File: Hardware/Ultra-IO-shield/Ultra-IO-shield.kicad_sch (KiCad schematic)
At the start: 88 parts, among them J1 Conn_01x04, J10 ASSMANN_A-DF_09_PP/Z, J11 TC_1578891_SCART, J12 Conn_01x01, J13 Conn_01x02, J14 CUI_SD-50BV, J15 Conn_01x02, J16 CUI_SD-50BV, J17 CUI_SD-50BV, J18 Conn_01x04, J19 Conn_01x04, J2 DIN-8_SD-80BV, J20 Conn_01x02, J21 ASSMANN_A-DF_09_PP/Z, J22 Conn_01x02, J3 Conn_01x04, J4 Conn_01x06, J5 Conn_01x02, J6 Conn_RCJ-023, J7 Conn_RCJ-022, J8 Conn_01x02, J9 NorComp_111-014-213L001, Q1 MMBT2907AM3T5G, U1 LM211, U2 AP7370, U3 ADuM226

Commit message: Redesigning of the IO-shield, to make room for Keyboard, power and USB.
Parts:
- added C?: C_GRM21BR61A476ME15K, Capacitor_SMD:C_0805_2012Metric, symbol LRJ-parts:C_GRM21BR61A476ME15K
- added J?: AdamTech_USB3-2_USB_C_Receptacle, LRJ:USB_3-2_Receptacle_A3-C31-D-RA-CS1, symbol LRJ-parts:AdamTech_USB3-2_USB_C_Receptacle
- added R?: R_ERJ-3GEYJ105V, Resistor_SMD:R_0603_1608Metric, symbol LRJ-parts:R_ERJ-3GEYJ105V
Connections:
- net +5V: now also J?.1 (VBUS[1]), J?.A4 (VBUS[2]), J?.A9 (VBUS), J?.B4 (VBUS), J?.B9 (VBUS)
- net GND: now also C?.2, J?.7 (DRAIN), R?.1
- new net: J?.4 (GND), J?.A1 (GND), J?.A12 (GND), J?.B1 (GND), J?.B12 (GND), R?.2
- new net: C?.1, J?.SH (SHIELD)
- new net AUX+: J?.A8 (SBU1)
- new net AUX-: J?.B8 (SBU2)
- new net CC1/HPD: J?.A5 (CC1)
- new net RX1+: J?.B11 (RX1+)
- new net RX1-: J?.B10 (RX1-)
- new net SSRX+: J?.6 (SSRX+)
- new net SSRX-: J?.5 (SSRX-)
- new net SSTX+: J?.9 (SSTX+)
- new net SSTX-: J?.8 (SSTX-)
- new net TX1+: J?.A2 (TX1+)
- new net TX1-: J?.A3 (TX1-)
- new net USB1_D+: J?.3 (D+)
- new net USB1_D-: J?.2 (D-)
- new net USB2_D+: J?.A7 (D-)
- new net USB2_D-: J?.A6 (D+)
- no-connect marks 21 -> 28
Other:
- note added: "USB connector"

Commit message: Multiple redesigns of the IO-shield. Replaced FPGA with lower pin-count AT10K, since the higher pin-count one is now obsolete.
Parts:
- removed J13, J20: Conn_01x02, Connector_PinHeader_1.27mm:PinHeader_1x02_P1.27mm_Horizontal, symbol Connector_Generic:Conn_01x02
- removed J4: Conn_01x06, Connector_PinHeader_1.27mm:PinHeader_1x06_P1.27mm_Horizontal, symbol Connector_Generic:Conn_01x06
- removed J?: AdamTech_USB3-2_USB_C_Receptacle, LRJ:USB_3-2_Receptacle_A3-C31-D-RA-CS1, symbol LRJ-parts:AdamTech_USB3-2_USB_C_Receptacle
- removed TP1, TP2: TestPoint_2Pole, NetTie:NetTie-2_SMD_Pad0.5mm, symbol Connector:TestPoint_2Pole
- added C14, C16: C_CL10B104KB8NNNL, LRJ:C_0603_1608Metric_round_court, symbol LRJ-parts:C_CL10B104KB8NNNL
- added C15: C_GRM21BR61A476ME15K, Capacitor_SMD:C_0805_2012Metric, symbol LRJ-parts:C_GRM21BR61A476ME15K
- added F2, F3: PPTC_0603L075, Fuse:Fuse_0603_1608Metric, symbol LRJ-parts:PPTC_0603L075
- added J13: Conn_01x01, LRJ:PinHeader_1x01_P2.54mm_Horizontal_less-silk, symbol Connector_Generic:Conn_01x01
- added J20, J29, J31, J32, J4: Conn_01x02, LRJ:PinHeader_1x01_P1.27mm_Horizontal_less-silk, symbol Connector_Generic:Conn_01x01
- added J23, J24: USB_C_GCT_USB4115-03-C, LRJ:USB_C_Receptacle_GCT_USB4115-03-C, symbol LRJ-parts:USB_C_GCT_USB4115-03-C
- added J25: Conn_01x02, LRJ:PinHeader_1x02_P1.27mm_Horizontal_less-silk, symbol Connector_Generic:Conn_01x02
- added J26, J27, J28, J30: BC075-06, LRJ:GCT_BC075-06_PinHeader_1x06_P1.00mm_Horizontal_SMD, symbol LRJ-parts:BC075-06
- added R40: R_ERJ-3GEYJ105V, Resistor_SMD:R_0603_1608Metric, symbol LRJ-parts:R_ERJ-3GEYJ105V
- added TP1, TP2: NetTie-2_small_round, NetTie:NetTie-2_SMD_Pad0.5mm, symbol LRJ-parts:NetTie-2_small_round
- C1, C12, C3, C5, C7: Mounting Type SMD -> (none); Mounting type (none) -> SMD; Voltage Rating (none) -> 50V; Voltage Rating  50V -> (none)
- C11, C9: value C -> 22nF
- C13: renamed from C?; Capacitance (none) -> 47uF; Capacity 47uF -> (none)
- F1: footprint Fuse:Fuse_1812_4532Metric -> LRJ:Yageo_Fuse_1812_4532Metric
- J12: footprint Connector_PinHeader_1.27mm:PinHeader_1x01_P1.27mm_Horizontal -> LRJ:PinHeader_1x01_P2.54mm_Horizontal_less-silk
- J15: footprint Connector_PinHeader_1.27mm:PinHeader_1x02_P1.27mm_Horizontal -> LRJ:PinHeader_1x01_P1.27mm_Horizontal_less-silk; symbol Connector_Generic:Conn_01x02 -> Connector_Generic:Conn_01x01
- J19: value Conn_01x04 -> Conn_01x03; footprint LRJ:PinHeader_1x04_P2.54mm_Horizontal_less-silk -> LRJ:PinHeader_1x03_P2.54mm_Horizontal_less-silk; symbol Connector_Generic:Conn_01x04 -> Connector_Generic:Conn_01x03
- J22, J5, J8: footprint Connector_PinHeader_1.27mm:PinHeader_1x02_P1.27mm_Horizontal -> LRJ:PinHeader_1x02_P1.27mm_Horizontal_less-silk
- R11, R23: value R -> 1K
- R12: value R -> 220K; footprint Resistor_SMD:R_0805_2012Metric -> LRJ:R_0805_2012Metric_roundcourt
- R13, R21, R22: value R -> 4.7K
- R14, R18: value R -> 10K
- R15, R16: value R -> 2.7K
- R17: value R -> 470K
- R20: value R -> 100R
- R8: footprint Resistor_SMD:R_0603_1608Metric -> LRJ:C_0603_1608Metric_round_court
- U3: footprint Package_SO:SOIC-8_7.5x5.85mm_P1.27mm -> LRJ:TEXAS_RI-8-1_7.5x5.85mm_P1.27mm
- gave numbers to parts that had none: 1
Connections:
- net +12V: now also J13.1 (Pin_1); no longer J19.1 (Pin_1)
- net +5V: now also J19.1 (Pin_1), C14.1, C16.1, F2.2, F3.2, J25.1 (Pin_1); no longer J15.2 (Pin_2), J19.2 (Pin_2)
- net +5VD: now also TP2.2
- net +5VD_: now also TP2.1
- net CC1/HPD: now also J23.A5 (CC1), J23.B5 (CC2), J27.2 (Pin_2)
- net GND: now also C14.2, C15.2, C16.2, J25.2 (Pin_2), J27.1 (Pin_1), J4.1 (Pin_1), R40.1, TP1.1
- net JOY_OUT_A: now also J28.2 (Pin_2)
- net JOY_OUT_B: now also J30.2 (Pin_2)
- net MID_RX: now also J32.1 (Pin_1)
- net MID_TX: now also J20.1 (Pin_1)
- net PD7: now also J19.3 (Pin_3); no longer J19.4 (Pin_4)
- net PRT_BUSY: now also J19.2 (Pin_2); no longer J19.3 (Pin_3)
- net RX1+: now also J23.B11 (RX1+), J26.4 (Pin_4)
- net RX1-: now also J23.B10 (RX1-), J26.3 (Pin_3)
- net USB1_D+: now also J23.A7 (D1-), J23.B7 (D2-), J26.1 (Pin_1)
- net USB1_D-: now also J23.A6 (D1+), J23.B6 (D2+), J26.2 (Pin_2)
- net USB2_D+: now also J24.A6 (D1+), J24.B6 (D2+), J27.6 (Pin_6)
- net USB2_D-: now also J24.A7 (D1-), J24.B7 (D2-), J27.5 (Pin_5)
- net ~{BCK_A}: now also J28.5 (Pin_5)
- net ~{BCK_B}: now also J30.4 (Pin_4)
- net ~{FWD_A}: now also J29.1 (Pin_1)
- net ~{FWD_B}: now also J31.1 (Pin_1)
- net ~{LFT_A}: now also J28.4 (Pin_4)
- net ~{LFT_B}: now also J30.3 (Pin_3)
- net ~{RGT_A}: now also J28.1 (Pin_1)
- net ~{RGT_B}: now also J30.1 (Pin_1)
- net ~{TRG1_A}: now also J28.6 (Pin_6)
- net ~{TRG1_B}: now also J30.6 (Pin_6)
- net ~{TRG2_A}: now also J28.3 (Pin_3)
- net ~{TRG2_B}: now also J30.5 (Pin_5)
- net at U3.6 (VOB): now also TP1.2
- net at R39.2: now also J23.SH (SHIELD)
- net GND_U: now reaches C13.1
- net GND_U: now also C15.1, J23.A1 (GND), J23.A12 (GND), J23.B1 (GND), J23.B12 (GND), J24.A1 (GND), J24.A12 (GND), J24.B1 (GND), J24.B12 (GND)
- new net: J24.SH (SHIELD), R40.2
- new net RX2+: J23.A11 (RX2+), J27.3 (Pin_3)
- new net RX2-: J23.A10 (RX2-), J27.4 (Pin_4)
- new net SBU1/AUX1+: J23.A8 (SBU1), J26.6 (Pin_6)
- new net SBU2/AUX1-: J23.B8 (SBU2), J26.5 (Pin_5)
- new net VBUS1: F2.1, J23.A4 (VBUS), J23.A9 (VBUS), J23.B4 (VBUS), J23.B9 (VBUS)
- new net VBUS2: F3.1, J24.A4 (VBUS), J24.A9 (VBUS), J24.B4 (VBUS), J24.B9 (VBUS)
- no-connect marks 28 -> 37
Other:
- note added: "Joysticks"
- note added: "Maximum USB path-length: 85 mm. USB-C alt-modes: Display Port Debug Accessory Mode (JTAG) HDMI Thunderbolt (ethernet)"
- note added: "PRINTER-nets"
- note added: "USB connectors"
- note added: "USB-C signals: ---- D1+- & D2+- = USB2.0, double for flipping. (con. together) CC1 & CC2 = Configuration Channels: HPD, interface config. & VCONN(5v or 6-20V) AUX/SBU = Auxiliary signals, alt-mode, Side-Band Use"
- note added: "USB-JTAG: --------- RX1- = SWDCLK RX1+ = SWDIO RX2- = SWO RX2+ = nReSeT SBU1 = VCC(target) SBU2 = GND"
- note added: "VBUSx = +5V to the USB-bus"
- note removed: "Pin_12"
- moved on the sheet: C1, C10, C100, C11, C12, C13, C2, C3, C4, C5, C6, C7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

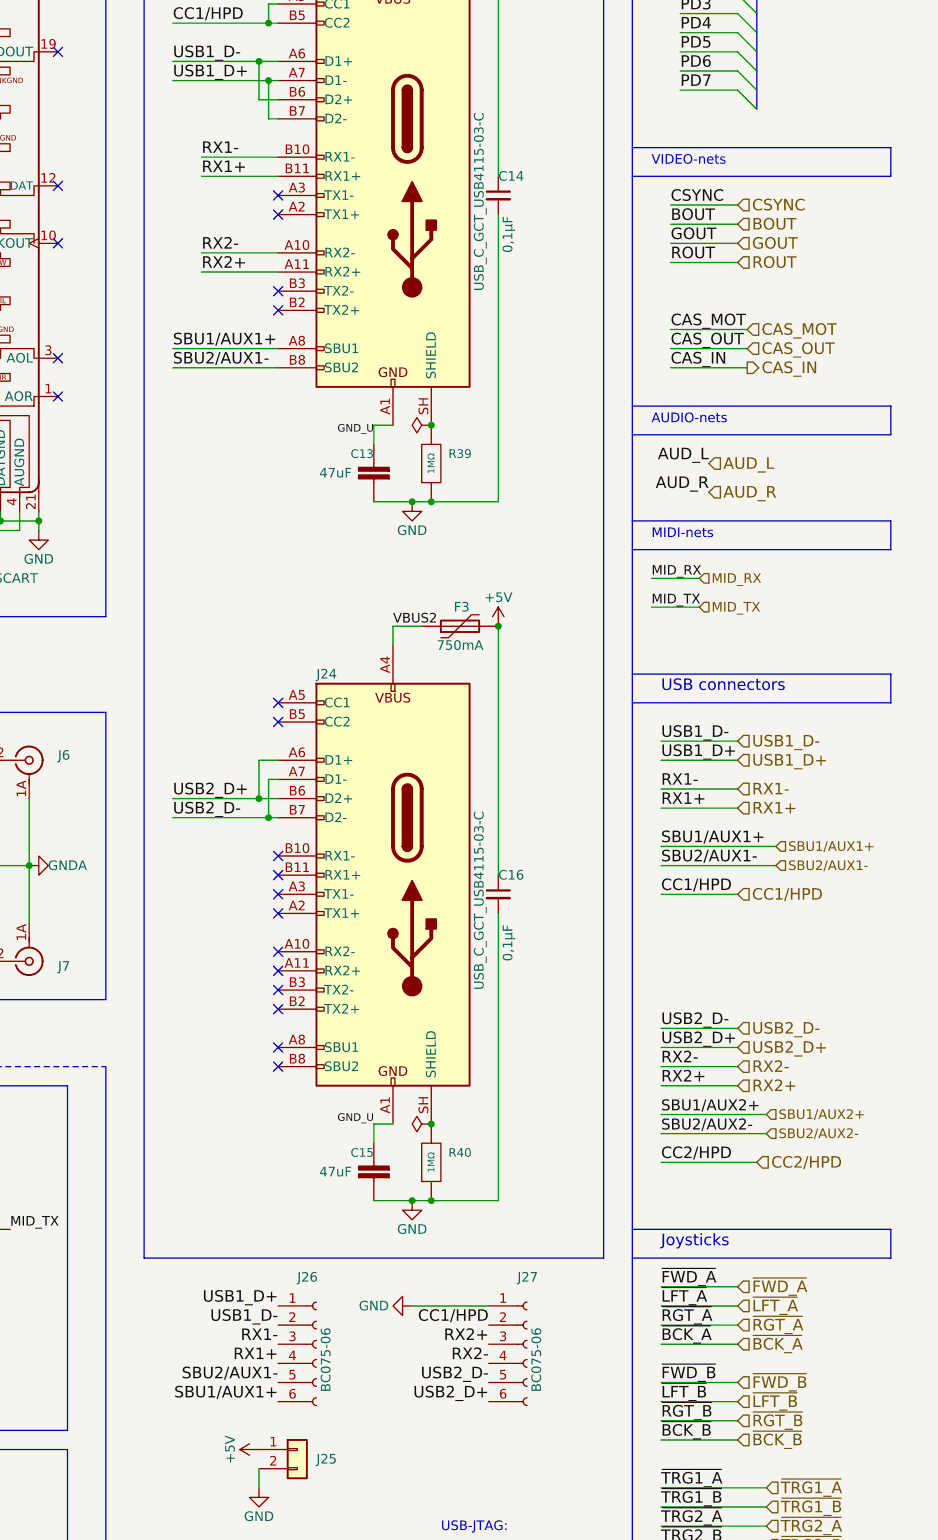
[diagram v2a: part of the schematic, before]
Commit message: Added cooler and CPU-mount footprints, as well as Indication LEDs.
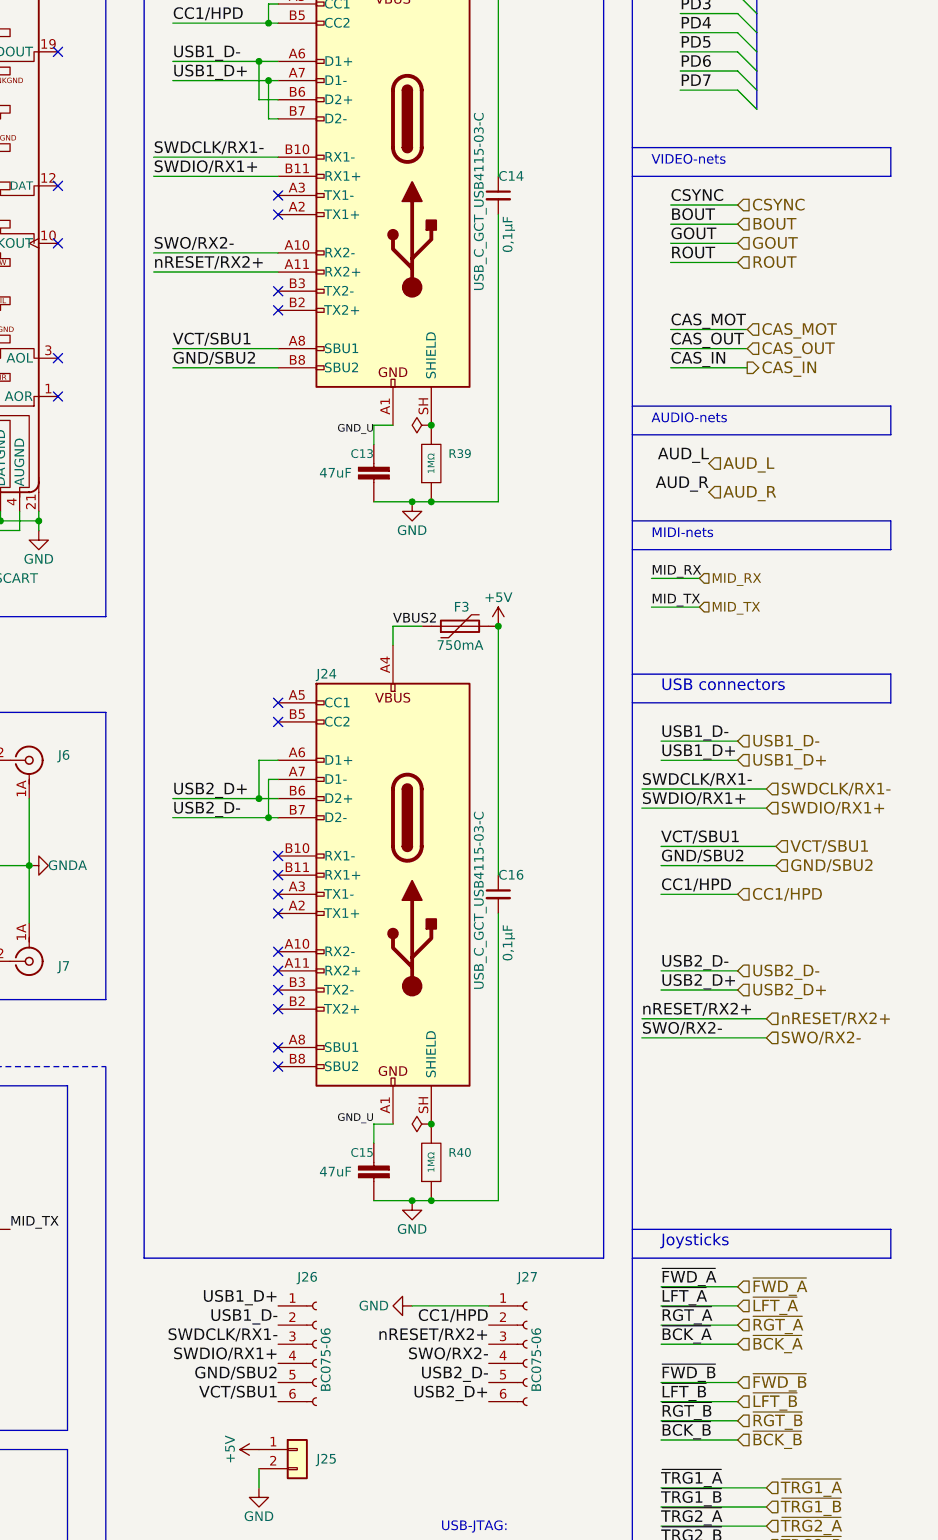
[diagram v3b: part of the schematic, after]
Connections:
- net RX1+ renamed SWDIO/RX1+
- net RX1- renamed SWDCLK/RX1-
- net RX2+ renamed nRESET/RX2+
- net RX2- renamed SWO/RX2-
- net SBU1/AUX1+ renamed VCT/SBU1
- net SBU2/AUX1- renamed GND/SBU2

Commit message: Started fixing many small issues.
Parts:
- removed TP2: NetTie-2_small_round, NetTie:NetTie-2_SMD_Pad0.5mm, symbol LRJ-parts:NetTie-2_small_round
- added C17: C_CL10B104KB8NNNL, Capacitor_SMD:C_0603_1608Metric_Pad1.08x0.95mm_HandSolder, symbol LRJ-parts:C_CL10B104KB8NNNL
- added J33: Conn_01x02, LRJ:PinHeader_1x01_P1.27mm_Horizontal_less-silk, symbol Connector_Generic:Conn_01x01
- added R41: R_ERJ-3GEYJ105V, Resistor_SMD:R_0603_1608Metric, symbol LRJ-parts:R_ERJ-3GEYJ105V
- J23, J24: footprint LRJ:USB_C_Receptacle_GCT_USB4115-03-C -> LRJ:GCT_USB4115-03-C_modified
- J26, J27, J28, J30: footprint LRJ:GCT_BC075-06_PinHeader_1x06_P1.00mm_Horizontal_SMD -> LRJ:GCT_BC075-06_PinHeader_1x06_P1.00mm_Horizontal_SMD_less-silk
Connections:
- net +5VD_ is gone; now on net +5VD: U2.3 (VOUT), U3.1 (VDD1)
- net GNDA is gone; now on net GND: J11.13 (RGND), J11.17 (VGND), J11.4 (AUGND), J11.5 (BGND), J11.9 (GGND), J3.1 (Pin_1), J3.2 (Pin_2), J6.1A (IN1), J6.1B (IN1), J7.1A (IN1), J7.1B (IN1), R24.2, R25.1
- net +12V-1K: now also C17.1
- net GND: now also C17.2, R41.2; no longer J11.21 (SH), J9.14 (Pin_14)
- net at J9.15 (SH), R100.2: now also J9.16 (SH2); no longer C100.1
- net SH1: now reaches J23.SH (SHIELD), R39.2
- net SH2: now reaches J24.SH (SHIELD), R40.2
- net 2.5V renamed BLANK
- net BLANK: now also J33.1 (Pin_1)
- net Earth renamed GND2
- new net: C100.1, J9.14 (Pin_14)
- new net SH3: J11.21 (SH), R41.1
- no-connect marks 37 -> 36
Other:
- note added: "Pin_56"
- moved on the sheet: C100, C5, C8, J12, J22, J8, R10, TP1
